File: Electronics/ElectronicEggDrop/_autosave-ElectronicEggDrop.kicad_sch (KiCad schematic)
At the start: 13 parts

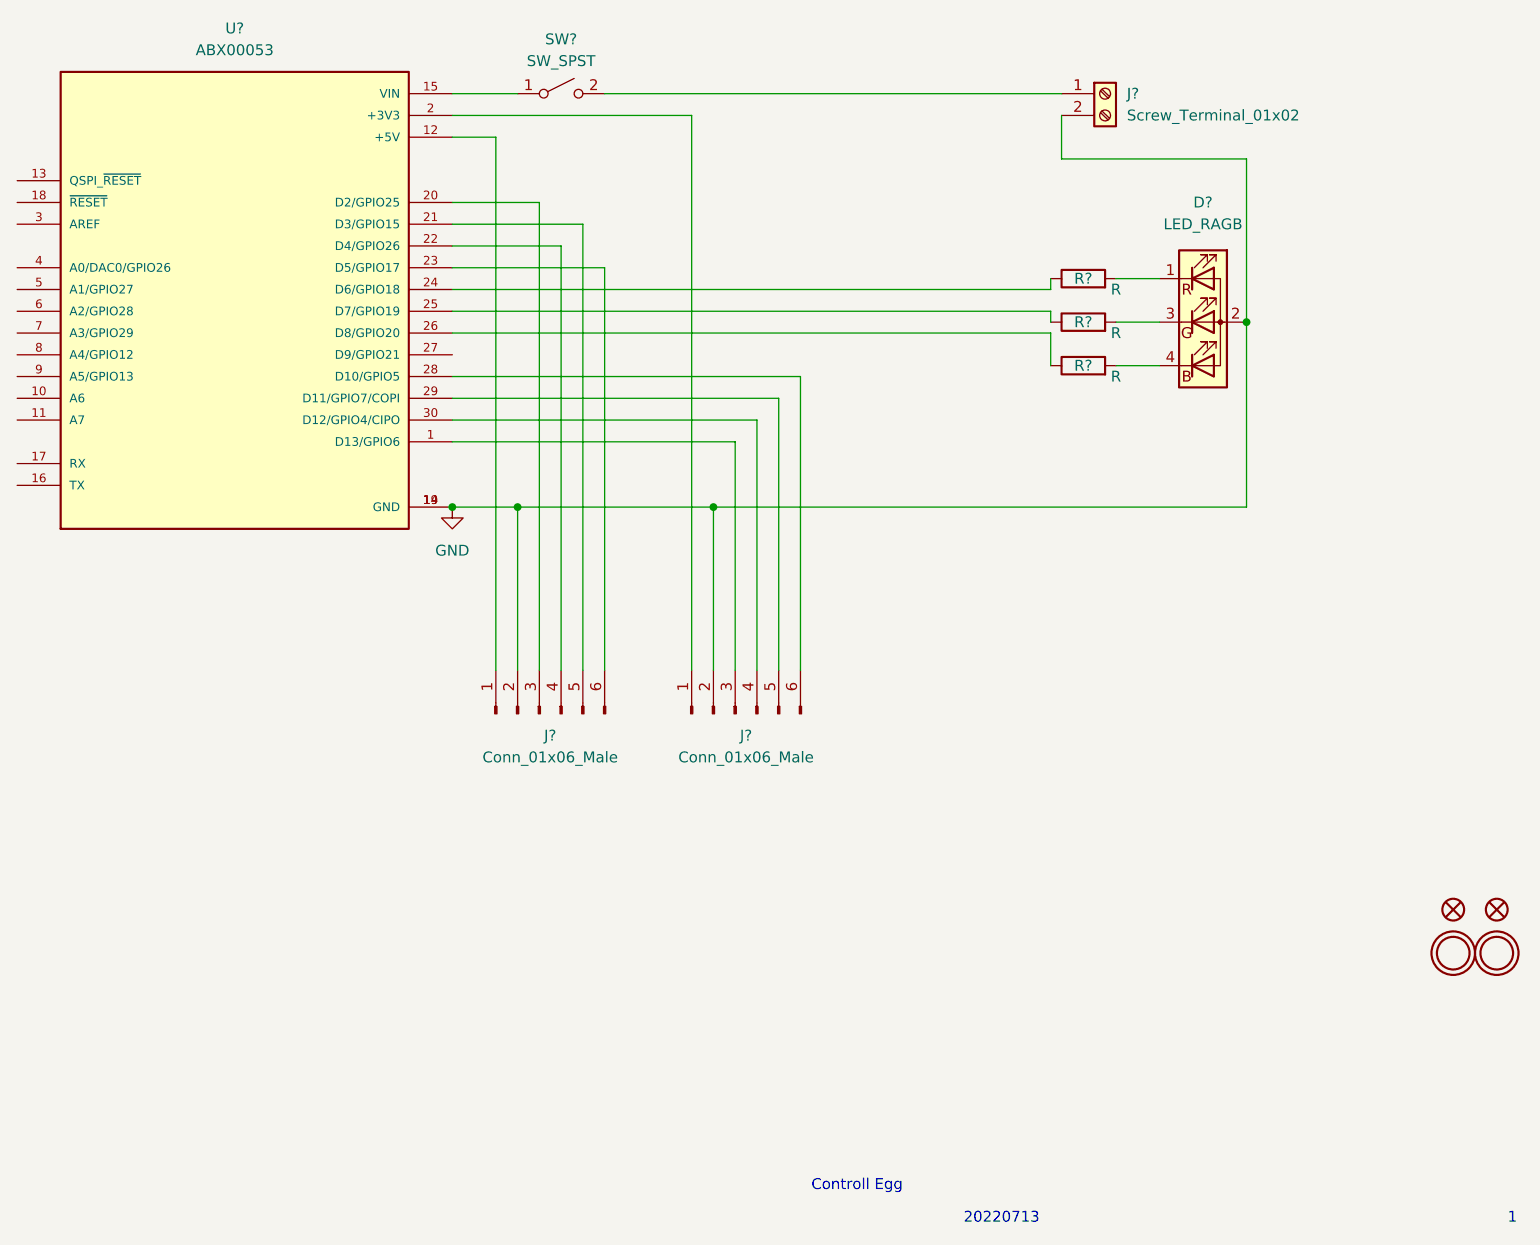
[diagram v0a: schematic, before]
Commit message: Created Egg Main board, needs different power connector. Needs secondary board
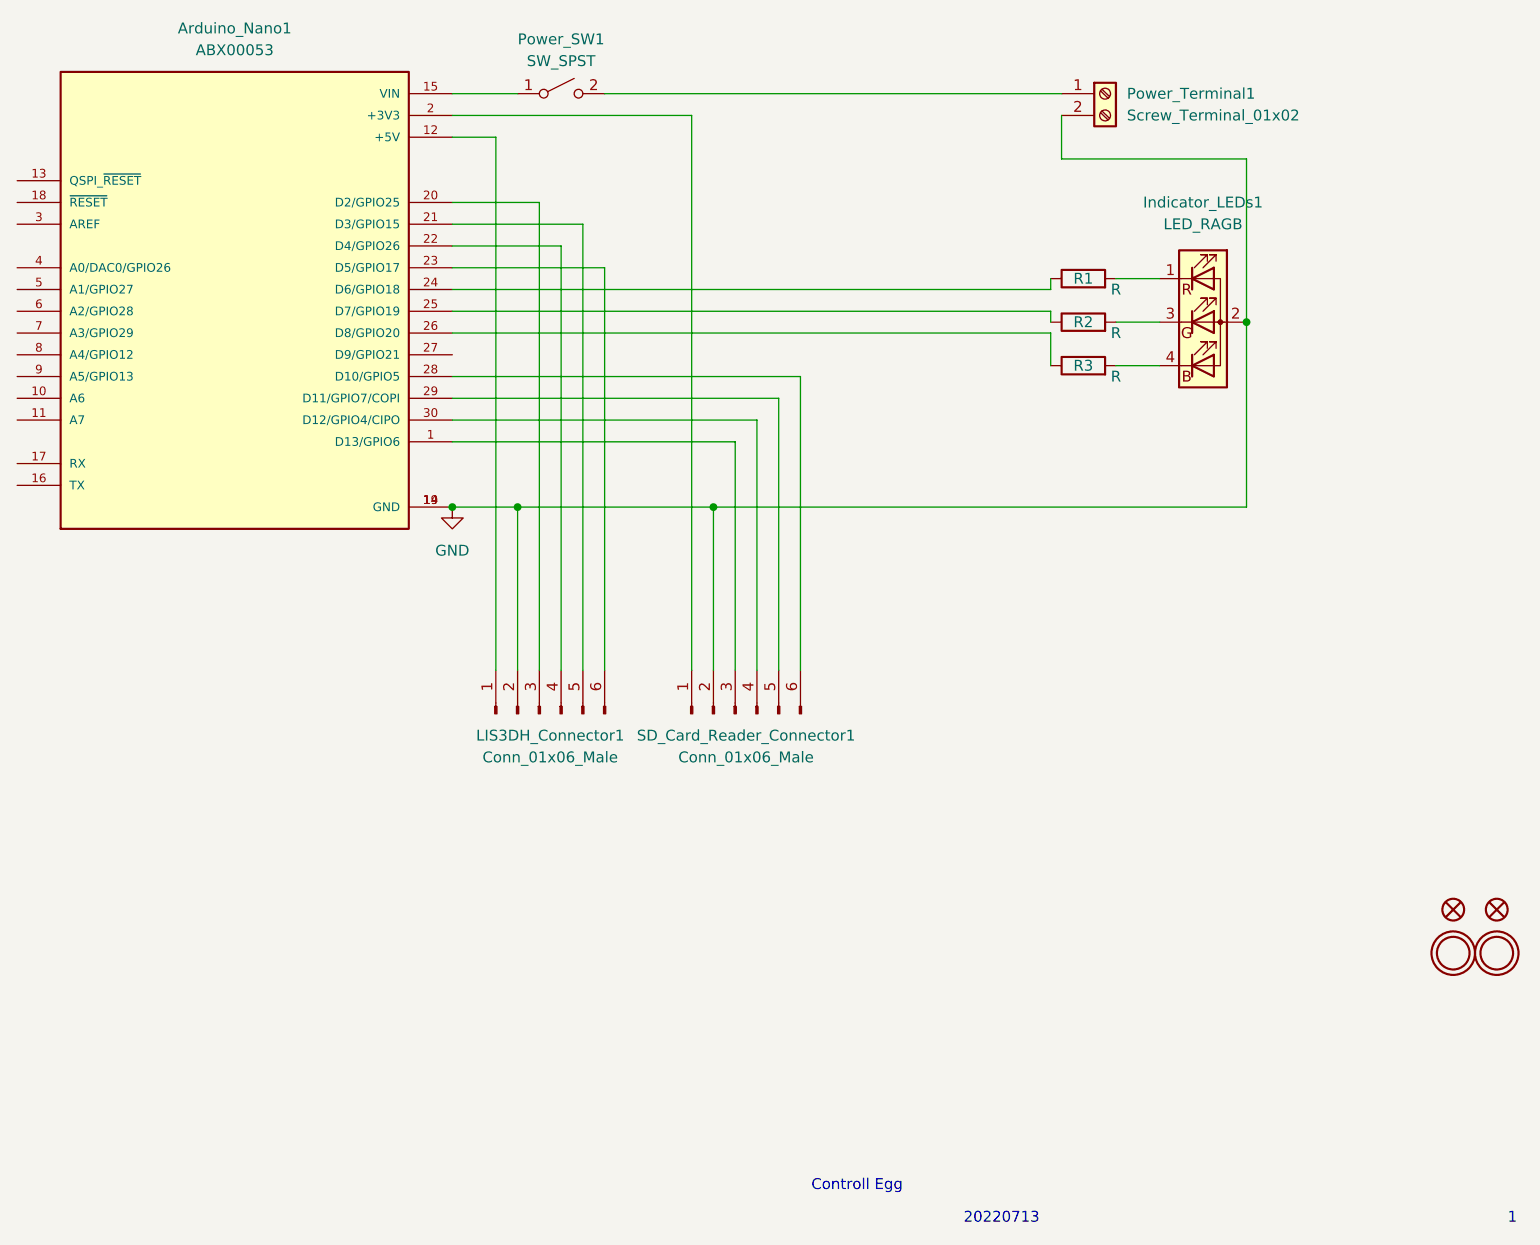
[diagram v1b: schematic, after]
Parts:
- Indicator_LEDs1: renamed from D?; footprint Connector_Molex:Molex_Mega-Fit_76829-0106_2x03_P5.70mm_Vertical -> Connector_Molex:Molex_KK-254_AE-6410-04A_1x04_P2.54mm_Vertical
- Power_SW1: renamed from SW?; footprint (none) -> Connector_Molex:Molex_KK-254_AE-6410-02A_1x02_P2.54mm_Vertical
- Power_Terminal1: renamed from J?; footprint (none) -> TerminalBlock_Phoenix:TerminalBlock_Phoenix_MPT-0,5-2-2.54_1x02_P2.54mm_Horizontal
- gave numbers to parts that had none: 6
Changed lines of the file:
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@@
   (symbol (lib_id "Device:R") (at 220.98 101.6 90) (unit 1)
     (in_bom yes) (on_board yes)
-    (property "Reference" "R?" (id 0) (at 220.98 101.6 90))
+    (property "Reference" "R3" (id 0) (at 220.98 101.6 90))
     (property "Value" "R" (id 1) (at 224.79 102.87 90))
     (property "Footprint" "Resistor_THT:R_Axial_DIN0204_L3.6mm_D1.6mm_P5.08mm_Horizontal" (id 2) (at 220.98 103.378 90)
@@
   (symbol (lib_id "Device:R") (at 220.98 91.44 90) (unit 1)
     (in_bom yes) (on_board yes)
-    (property "Reference" "R?" (id 0) (at 220.98 91.44 90))
+    (property "Reference" "R1" (id 0) (at 220.98 91.44 90))
     (property "Value" "R" (id 1) (at 224.79 92.71 90))
     (property "Footprint" "Resistor_THT:R_Axial_DIN0204_L3.6mm_D1.6mm_P5.08mm_Horizontal" (id 2) (at 220.98 93.218 90)
@@
   (symbol (lib_id "Switch:SW_SPST") (at 160.02 69.85 0) (unit 1)
     (in_bom yes) (on_board yes) (fields_autoplaced)
-    (property "Reference" "SW?" (id 0) (at 160.02 63.5 0))
+    (property "Reference" "Power_SW1" (id 0) (at 160.02 63.5 0))
     (property "Value" "SW_SPST" (id 1) (at 160.02 66.04 0))
-    (property "Footprint" "" (id 2) (at 160.02 69.85 0)
+    (property "Footprint" "Connector_Molex:Molex_KK-254_AE-6410-02A_1x02_P2.54mm_Vertical" (id 2) (at 160.02 69.85 0)
       (effects (font (size 1.27 1.27)) hide)
     )
@@
   (symbol (lib_id "Connector:Conn_01x06_Male") (at 157.48 142.24 90) (unit 1)
     (in_bom yes) (on_board yes) (fields_autoplaced)
-    (property "Reference" "J?" (id 0) (at 158.75 144.78 90))
+    (property "Reference" "LIS3DH_Connector1" (id 0) (at 158.75 144.78 90))
     (property "Value" "Conn_01x06_Male" (id 1) (at 158.75 147.32 90))
     (property "Footprint" "Connector_Molex:Molex_KK-254_AE-6410-06A_1x06_P2.54mm_Vertical" (id 2) (at 157.48 142.24 0)
@@
   (symbol (lib_id "Device:R") (at 220.98 96.52 90) (unit 1)
     (in_bom yes) (on_board yes)
-    (property "Reference" "R?" (id 0) (at 220.98 96.52 90))
+    (property "Reference" "R2" (id 0) (at 220.98 96.52 90))
     (property "Value" "R" (id 1) (at 224.79 97.79 90))
     (property "Footprint" "Resistor_THT:R_Axial_DIN0204_L3.6mm_D1.6mm_P5.08mm_Horizontal" (id 2) (at 220.98 98.298 90)
@@
   (symbol (lib_id "power:GND") (at 147.32 118.11 0) (unit 1)
     (in_bom yes) (on_board yes) (fields_autoplaced)
-    (property "Reference" "#PWR?" (id 0) (at 147.32 124.46 0)
+    (property "Reference" "#PWR0101" (id 0) (at 147.32 124.46 0)
       (effects (font (size 1.27 1.27)) hide)
     )
@@
   (symbol (lib_id "Connector:Screw_Terminal_01x02") (at 223.52 69.85 0) (unit 1)
     (in_bom yes) (on_board yes) (fields_autoplaced)
-    (property "Reference" "J?" (id 0) (at 226.06 69.8499 0)
+    (property "Reference" "Power_Terminal1" (id 0) (at 226.06 69.8499 0)
       (effects (font (size 1.27 1.27)) (justify left))
     )
@@
       (effects (font (size 1.27 1.27)) (justify left))
     )
-    (property "Footprint" "" (id 2) (at 223.52 69.85 0)
+    (property "Footprint" "TerminalBlock_Phoenix:TerminalBlock_Phoenix_MPT-0,5-2-2.54_1x02_P2.54mm_Horizontal" (id 2) (at 223.52 69.85 0)
       (effects (font (size 1.27 1.27)) hide)
     )
@@
   (symbol (lib_id "Connector:Conn_01x06_Male") (at 180.34 142.24 90) (unit 1)
     (in_bom yes) (on_board yes) (fields_autoplaced)
-    (property "Reference" "J?" (id 0) (at 181.61 144.78 90))
+    (property "Reference" "SD_Card_Reader_Connector1" (id 0) (at 181.61 144.78 90))
     (property "Value" "Conn_01x06_Male" (id 1) (at 181.61 147.32 90))
     (property "Footprint" "Connector_Molex:Molex_KK-254_AE-6410-06A_1x06_P2.54mm_Vertical" (id 2) (at 180.34 142.24 0)
@@
   (symbol (lib_id "ABX00053:ABX00053") (at 121.92 92.71 0) (unit 1)
     (in_bom yes) (on_board yes) (fields_autoplaced)
-    (property "Reference" "U?" (id 0) (at 121.92 62.23 0))
+    (property "Reference" "Arduino_Nano1" (id 0) (at 121.92 62.23 0))
     (property "Value" "ABX00053" (id 1) (at 121.92 64.77 0))
     (property "Footprint" "MODULE_ABX00053" (id 2) (at 121.92 92.71 0)
@@
   (symbol (lib_id "Device:LED_RAGB") (at 234.95 96.52 0) (unit 1)
     (in_bom yes) (on_board yes) (fields_autoplaced)
-    (property "Reference" "D?" (id 0) (at 234.95 82.55 0))
+    (property "Reference" "Indicator_LEDs1" (id 0) (at 234.95 82.55 0))
     (property "Value" "LED_RAGB" (id 1) (at 234.95 85.09 0))
-    (property "Footprint" "Connector_Molex:Molex_Mega-Fit_76829-0106_2x03_P5.70mm_Vertical" (id 2) (at 234.95 97.79 0)
+    (property "Footprint" "Connector_Molex:Molex_KK-254_AE-6410-04A_1x04_P2.54mm_Vertical" (id 2) (at 234.95 97.79 0)
       (effects (font (size 1.27 1.27)) hide)
     )
@@
   (symbol_instances
     (path "/af7d1780-278a-4463-9202-e431edff4abf"
-      (reference "#PWR?") (unit 1) (value "GND") (footprint "")
-    )
-    (path "/f7aa1d10-f8d1-4fe6-acb4-10abc2244f09"
-      (reference "D?") (unit 1) (value "LED_RAGB") (footprint "Connector_Molex:Molex_Mega-Fit_76829-0106_2x03_P5.70mm_Vertical")
+      (reference "#PWR0101") (unit 1) (value "GND") (footprint "")
+    )
+    (path "/e0dad96b-23b2-46bc-93d4-eedf18ddd013"
+      (reference "Arduino_Nano1") (unit 1) (value "ABX00053") (footprint "MODULE_ABX00053")
     )
     (path "/0ab1aabe-6d15-4feb-8511-7c76d8512d24"
@@
       (reference "FID2") (unit 1) (value "FIDUCIAL{dblquote}{dblquote}") (footprint "ElectronicEggDrop:FIDUCIAL_1MM")
     )
+    (path "/f7aa1d10-f8d1-4fe6-acb4-10abc2244f09"
+      (reference "Indicator_LEDs1") (unit 1) (value "LED_RAGB") (footprint "Connector_Molex:Molex_KK-254_AE-6410-04A_1x04_P2.54mm_Vertical")
+    )
     (path "/432a2ef5-8c4c-4a55-bf4b-ba5b90ca0b70"
-      (reference "J?") (unit 1) (value "Conn_01x06_Male") (footprint "Connector_Molex:Molex_KK-254_AE-6410-06A_1x06_P2.54mm_Vertical")
+      (reference "LIS3DH_Connector1") (unit 1) (value "Conn_01x06_Male") (footprint "Connector_Molex:Molex_KK-254_AE-6410-06A_1x06_P2.54mm_Vertical")
+    )
+    (path "/3bd3481f-6f6f-4cff-8d9c-7c9dc14e3fc3"
+      (reference "Power_SW1") (unit 1) (value "SW_SPST") (footprint "Connector_Molex:Molex_KK-254_AE-6410-02A_1x02_P2.54mm_Vertical")
     )
     (path "/c79642f2-5f2f-4055-93db-5cce65ec58b5"
-      (reference "J?") (unit 1) (value "Screw_Terminal_01x02") (footprint "")
+      (reference "Power_Terminal1") (unit 1) (value "Screw_Terminal_01x02") (footprint "TerminalBlock_Phoenix:TerminalBlock_Phoenix_MPT-0,5-2-2.54_1x02_P2.54mm_Horizontal")
+    )
+    (path "/27354c14-7ea3-4310-8f3a-463ad49a3e7f"
+      (reference "R1") (unit 1) (value "R") (footprint "Resistor_THT:R_Axial_DIN0204_L3.6mm_D1.6mm_P5.08mm_Horizontal")
+    )
+    (path "/83455da2-0ebd-405c-8668-8efde92b2d08"
+      (reference "R2") (unit 1) (value "R") (footprint "Resistor_THT:R_Axial_DIN0204_L3.6mm_D1.6mm_P5.08mm_Horizontal")
+    )
+    (path "/1cc56aee-2767-4a3b-9d4c-5a6627626533"
+      (reference "R3") (unit 1) (value "R") (footprint "Resistor_THT:R_Axial_DIN0204_L3.6mm_D1.6mm_P5.08mm_Horizontal")
     )
     (path "/c93ef0e7-749a-4bd6-b03c-c57ac7336301"
-      (reference "J?") (unit 1) (value "Conn_01x06_Male") (footprint "Connector_Molex:Molex_KK-254_AE-6410-06A_1x06_P2.54mm_Vertical")
-    )
-    (path "/1cc56aee-2767-4a3b-9d4c-5a6627626533"
-      (reference "R?") (unit 1) (value "R") (footprint "Resistor_THT:R_Axial_DIN0204_L3.6mm_D1.6mm_P5.08mm_Horizontal")
-    )
-    (path "/27354c14-7ea3-4310-8f3a-463ad49a3e7f"
-      (reference "R?") (unit 1) (value "R") (footprint "Resistor_THT:R_Axial_DIN0204_L3.6mm_D1.6mm_P5.08mm_Horizontal")
-    )
-    (path "/83455da2-0ebd-405c-8668-8efde92b2d08"
-      (reference "R?") (unit 1) (value "R") (footprint "Resistor_THT:R_Axial_DIN0204_L3.6mm_D1.6mm_P5.08mm_Horizontal")
-    )
-    (path "/3bd3481f-6f6f-4cff-8d9c-7c9dc14e3fc3"
-      (reference "SW?") (unit 1) (value "SW_SPST") (footprint "")
+      (reference "SD_Card_Reader_Connector1") (unit 1) (value "Conn_01x06_Male") (footprint "Connector_Molex:Molex_KK-254_AE-6410-06A_1x06_P2.54mm_Vertical")
     )
     (path "/1d853ae8-ce78-4e5a-8c2a-2d6b4dce02f7"
@@
       (reference "U$13") (unit 1) (value "MOUNTINGHOLE2.5") (footprint "ElectronicEggDrop:MOUNTINGHOLE_2.5_PLATED")
     )
-    (path "/e0dad96b-23b2-46bc-93d4-eedf18ddd013"
-      (reference "U?") (unit 1) (value "ABX00053") (footprint "MODULE_ABX00053")
-    )
-  )
+  )
